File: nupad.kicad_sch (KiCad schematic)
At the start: 1 part, among them U1 ATmega328P-P

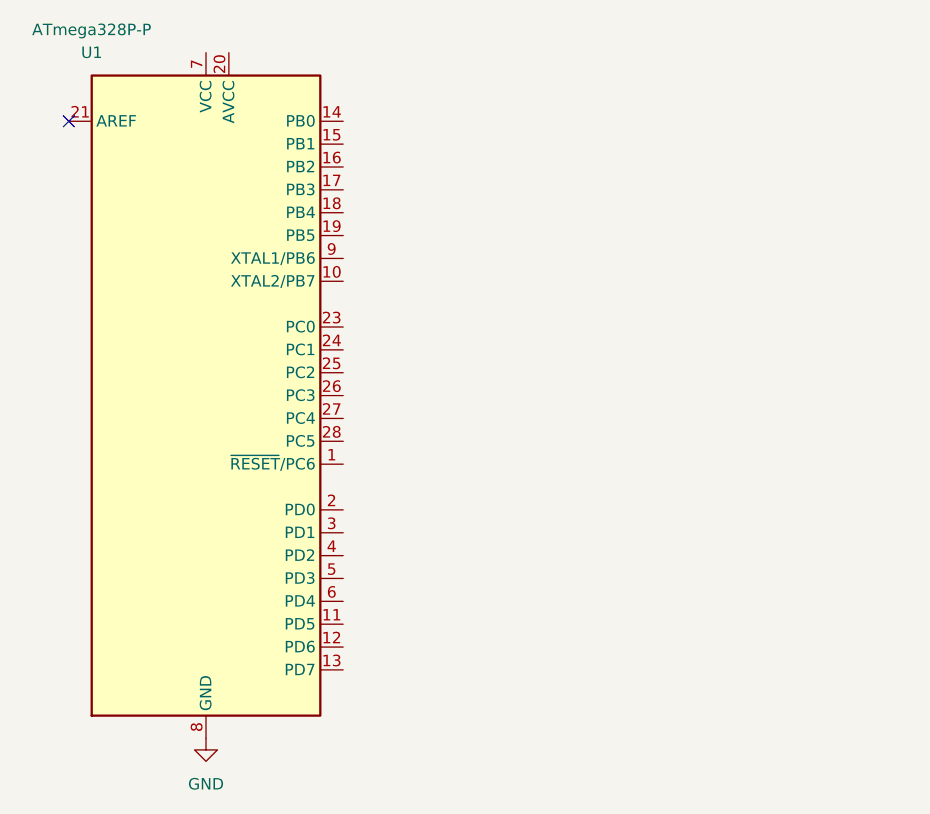
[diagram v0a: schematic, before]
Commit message: 스키메틱에 발진회로 추가
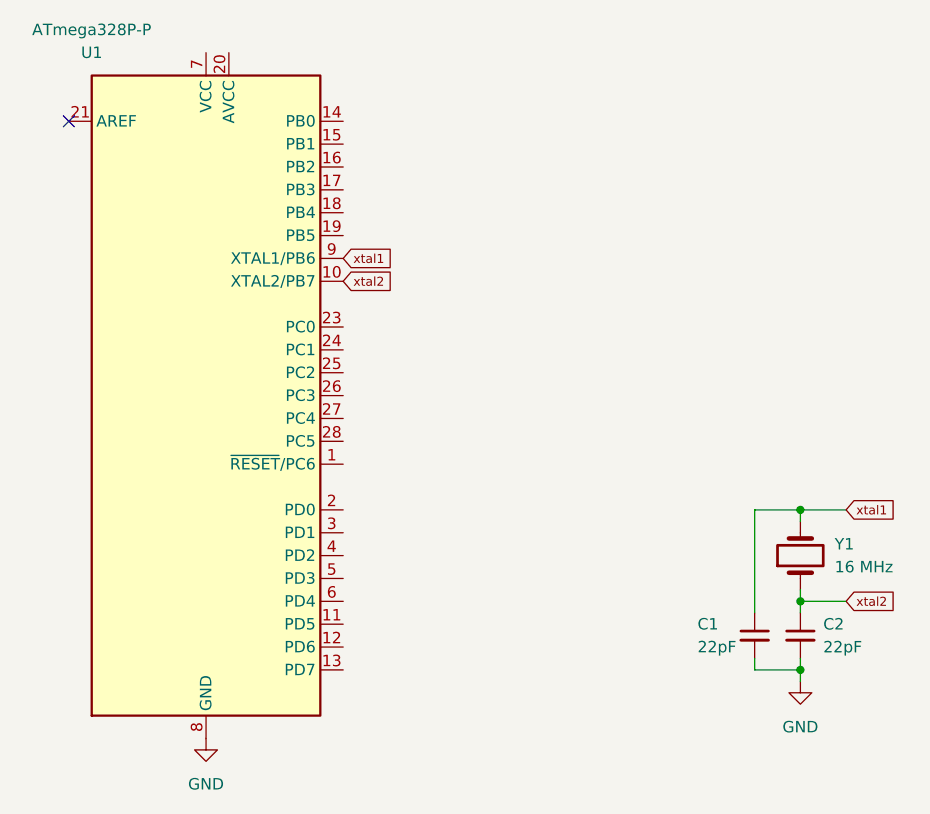
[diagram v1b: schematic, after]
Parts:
- added C1, C2: 22pF, symbol Device:C_Small
- added Y1: 16 MHz, symbol Device:Crystal
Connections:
- net GND: now also C1.2, C2.2
- net xtal2: now reaches U1.10 (XTAL2/PB7)
- net xtal2: now also C2.1, Y1.1
- net xtal1: now reaches U1.9 (XTAL1/PB6)
- net xtal1: now also C1.1, Y1.2
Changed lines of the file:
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@@
 (kicad_sch (version 20211123) (generator eeschema)
   (paper "A4")
+  (junction (at 99.06 162.56) (diameter 0) (color 0 0 0 0)
+  )
+  (junction (at 99.06 172.72) (diameter 0) (color 0 0 0 0)
+  )
+  (junction (at 99.06 180.34) (diameter 0) (color 0 0 0 0)
+  )
   (no_connect (at 17.78 119.38))
+  (wire (pts (xy 99.06 172.72) (xy 104.14 172.72))
+    (stroke (width 0) (type default) (color 0 0 0 0))
+  )
+  (wire (pts (xy 93.98 180.34) (xy 99.06 180.34))
+    (stroke (width 0) (type default) (color 0 0 0 0))
+  )
+  (wire (pts (xy 99.06 172.72) (xy 99.06 171.45))
+    (stroke (width 0) (type default) (color 0 0 0 0))
+  )
+  (wire (pts (xy 93.98 179.07) (xy 93.98 180.34))
+    (stroke (width 0) (type default) (color 0 0 0 0))
+  )
+  (wire (pts (xy 99.06 172.72) (xy 99.06 173.99))
+    (stroke (width 0) (type default) (color 0 0 0 0))
+  )
+  (wire (pts (xy 93.98 162.56) (xy 93.98 173.99))
+    (stroke (width 0) (type default) (color 0 0 0 0))
+  )
+  (wire (pts (xy 99.06 180.34) (xy 99.06 181.61))
+    (stroke (width 0) (type default) (color 0 0 0 0))
+  )
+  (wire (pts (xy 104.14 162.56) (xy 99.06 162.56))
+    (stroke (width 0) (type default) (color 0 0 0 0))
+  )
+  (wire (pts (xy 99.06 162.56) (xy 99.06 163.83))
+    (stroke (width 0) (type default) (color 0 0 0 0))
+  )
+  (wire (pts (xy 99.06 179.07) (xy 99.06 180.34))
+    (stroke (width 0) (type default) (color 0 0 0 0))
+  )
+  (wire (pts (xy 93.98 162.56) (xy 99.06 162.56))
+    (stroke (width 0) (type default) (color 0 0 0 0))
+  )
+  (global_label "xtal1" (shape input) (at 48.26 134.62 0) (fields_autoplaced)
+    (effects (font (size 1 1)) (justify left))
+    (property "Intersheet References" "${INTERSHEET_REFS}" (id 0) (at 53.9219 134.5575 0)
+      (effects (font (size 1 1)) (justify left) hide)
+    )
+  )
+  (global_label "xtal2" (shape input) (at 48.26 137.16 0) (fields_autoplaced)
+    (effects (font (size 1 1)) (justify left))
+    (property "Intersheet References" "${INTERSHEET_REFS}" (id 0) (at 53.9219 137.0975 0)
+      (effects (font (size 1 1)) (justify left) hide)
+    )
+  )
+  (global_label "xtal2" (shape input) (at 104.14 172.72 0) (fields_autoplaced)
+    (effects (font (size 1 1)) (justify left))
+    (property "Intersheet References" "${INTERSHEET_REFS}" (id 0) (at 109.8019 172.6575 0)
+      (effects (font (size 1 1)) (justify left) hide)
+    )
+  )
+  (global_label "xtal1" (shape input) (at 104.14 162.56 0) (fields_autoplaced)
+    (effects (font (size 1 1)) (justify left))
+    (property "Intersheet References" "${INTERSHEET_REFS}" (id 0) (at 109.8019 162.4975 0)
+      (effects (font (size 1 1)) (justify left) hide)
+    )
+  )
+  (symbol (lib_id "power:GND") (at 99.06 181.61 0) (unit 1)
+    (in_bom yes) (on_board yes) (fields_autoplaced)
+    (property "Reference" "#PWR?" (id 0) (at 99.06 187.96 0)
+      (effects (font (size 1.27 1.27)) hide)
+    )
+    (property "Value" "GND" (id 1) (at 99.06 186.69 0))
+    (property "Footprint" "" (id 2) (at 99.06 181.61 0)
+      (effects (font (size 1.27 1.27)) hide)
+    )
+    (property "Datasheet" "" (id 3) (at 99.06 181.61 0)
+      (effects (font (size 1.27 1.27)) hide)
+    )
+    (pin "1")
+  )
+  (symbol (lib_id "Device:C_Small") (at 99.06 176.53 0) (unit 1)
+    (in_bom yes) (on_board yes) (fields_autoplaced)
+    (property "Reference" "C2" (id 0) (at 101.6 175.2662 0)
+      (effects (font (size 1.27 1.27)) (justify left))
+    )
+    (property "Value" "22pF" (id 1) (at 101.6 177.8062 0)
+      (effects (font (size 1.27 1.27)) (justify left))
+    )
+    (property "Footprint" "" (id 2) (at 99.06 176.53 0)
+      (effects (font (size 1.27 1.27)) hide)
+    )
+    (property "Datasheet" "~" (id 3) (at 99.06 176.53 0)
+      (effects (font (size 1.27 1.27)) hide)
+    )
+    (pin "1")
+    (pin "2")
+  )
   (symbol (lib_id "MCU_Microchip_ATmega:ATmega328P-P") (at 33.02 149.86 0) (unit 1)
     (in_bom yes) (on_board yes)
@@
   (symbol (lib_id "power:GND") (at 33.02 187.96 0) (unit 1)
     (in_bom yes) (on_board yes) (fields_autoplaced)
-    (property "Reference" "#PWR?" (id 0) (at 33.02 194.31 0)
+    (property "Reference" "#PWR01" (id 0) (at 33.02 194.31 0)
       (effects (font (size 1.27 1.27)) hide)
     )
@@
     (pin "1")
   )
+  (symbol (lib_id "Device:C_Small") (at 93.98 176.53 0) (unit 1)
+    (in_bom yes) (on_board yes)
+    (property "Reference" "C1" (id 0) (at 87.63 175.26 0)
+      (effects (font (size 1.27 1.27)) (justify left))
+    )
+    (property "Value" "22pF" (id 1) (at 87.63 177.8 0)
+      (effects (font (size 1.27 1.27)) (justify left))
+    )
+    (property "Footprint" "" (id 2) (at 93.98 176.53 0)
+      (effects (font (size 1.27 1.27)) hide)
+    )
+    (property "Datasheet" "~" (id 3) (at 93.98 176.53 0)
+      (effects (font (size 1.27 1.27)) hide)
+    )
+    (pin "1")
+    (pin "2")
+  )
+  (symbol (lib_id "Device:Crystal") (at 99.06 167.64 90) (unit 1)
+    (in_bom yes) (on_board yes) (fields_autoplaced)
+    (property "Reference" "Y1" (id 0) (at 102.87 166.3699 90)
+      (effects (font (size 1.27 1.27)) (justify right))
+    )
+    (property "Value" "16 MHz" (id 1) (at 102.87 168.9099 90)
+      (effects (font (size 1.27 1.27)) (justify right))
+    )
+    (property "Footprint" "" (id 2) (at 99.06 167.64 0)
+      (effects (font (size 1.27 1.27)) hide)
+    )
+    (property "Datasheet" "~" (id 3) (at 99.06 167.64 0)
+      (effects (font (size 1.27 1.27)) hide)
+    )
+    (pin "1")
+    (pin "2")
+  )
   (sheet_instances
     (path "/" (page "1"))
@@
   (symbol_instances
     (path "/89ef3e43-38c1-4e6e-86ff-e90bda0f8f75"
+      (reference "#PWR01") (unit 1) (value "GND") (footprint "")
+    )
+    (path "/091cbf72-90fc-456c-8811-f9249ce880e7"
       (reference "#PWR?") (unit 1) (value "GND") (footprint "")
+    )
+    (path "/cf0edc33-d184-4c16-afa8-ae807c902458"
+      (reference "C1") (unit 1) (value "22pF") (footprint "")
+    )
+    (path "/4a9f9a71-1534-4d98-be37-07ddd5cb5656"
+      (reference "C2") (unit 1) (value "22pF") (footprint "")
     )
     (path "/54accfcc-330b-4c29-9949-badcdab1bacc"
       (reference "U1") (unit 1) (value "ATmega328P-P") (footprint "Package_DIP:DIP-28_W7.62mm")
     )
-  )
+    (path "/d3e19443-a155-48aa-a140-bbab9addf240"
+      (reference "Y1") (unit 1) (value "16 MHz") (footprint "")
+    )
+  )
